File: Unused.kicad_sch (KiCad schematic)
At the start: 1 part

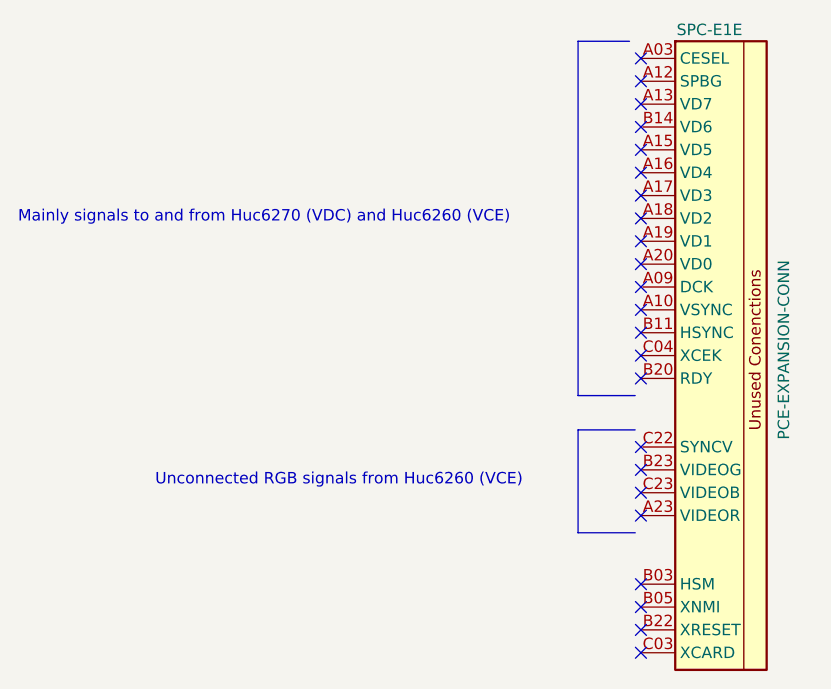
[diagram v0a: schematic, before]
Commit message: Fixed a few typos and mainly renamed connections to CD-ROM with more accurate descriptions
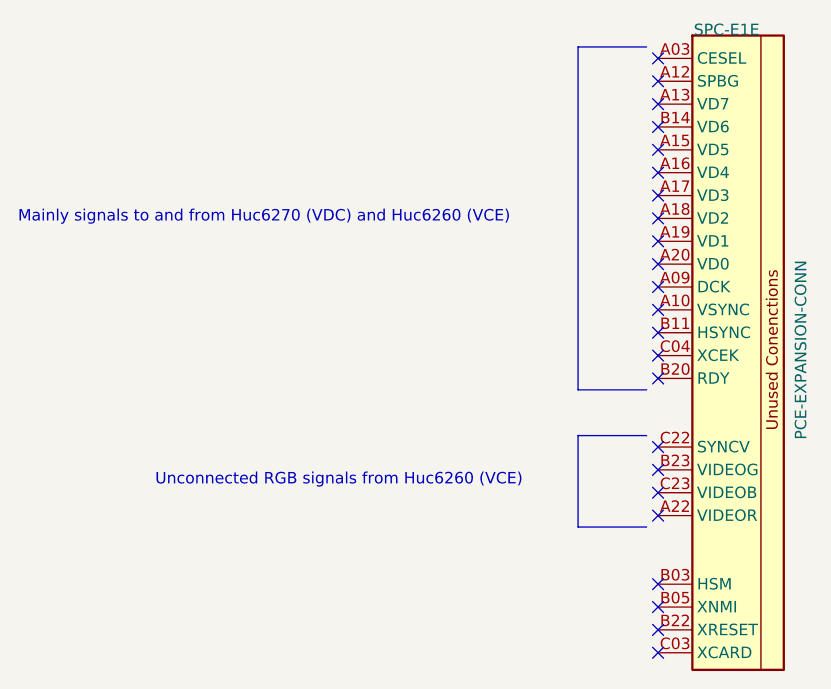
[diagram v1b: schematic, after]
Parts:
- SPC-E1: footprint (none) -> IFU-30:PinSocket_3x23_P2.54mm_Horizontal
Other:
- title: (none) -> NEC PC-Engine IFU-30
- moved on the sheet: SPC-E1E
